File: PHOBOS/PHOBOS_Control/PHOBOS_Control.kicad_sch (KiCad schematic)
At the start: 85 parts, among them J1 Screw_Terminal_01x02, J2 Conn_01x06, J3 Conn_Coaxial, J4 Conn_01x03, J5 Conn_01x03, J6 USB4056-03-A_REVA2, SW4 KMR211GLFS, U1 SX1280IMLTRT, U2 TLV9351IDCKR, U3 W25Q128JVSIQ, U4 NCP1117-3.3_SOT223, U5 RP2040, U6 TLV9351IDCKR, U7 TLV9351IDCKR, U8 TLV9351IDCKR, Y1 ABM8-272-T3, Y2 C1E-52.000-10-1012-X-M

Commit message: mounting holes added and shape changed. design blocks utilized
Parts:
- removed C26: .8P, Capacitor_SMD:C_0402_1005Metric_Pad0.74x0.62mm_HandSolder, symbol Device:C
- removed C27, C28: 100n, Capacitor_SMD:C_0402_1005Metric_Pad0.74x0.62mm_HandSolder, symbol Device:C
- removed C29: 100p, Capacitor_SMD:C_0402_1005Metric_Pad0.74x0.62mm_HandSolder, symbol Device:C
- removed C7: 1.2p, Capacitor_SMD:C_0402_1005Metric_Pad0.74x0.62mm_HandSolder, symbol Device:C
- removed J2: Conn_01x06, Connector_JST:JST_PH_B6B-PH-K_1x06_P2.00mm_Vertical, symbol Connector_Generic:Conn_01x06
- removed J3: Conn_Coaxial, SMA_J_P_GF_RA_SM1:SAMTEC_SMA-J-P-GF-RA-SM1, symbol Connector:Conn_Coaxial
- removed Y2: C1E-52.000-10-1012-X-M, C1E-52.000-10-1012-X-M:XTAL_C1E-52.000-10-1012-X-M, symbol C1E-52.000-10-1012-X-M:C1E-52.000-10-1012-X-M
- added C0: .8P, Capacitor_SMD:C_0402_1005Metric_Pad0.74x0.62mm_HandSolder, symbol Device:C
- added C1: 1.2p, Capacitor_SMD:C_0402_1005Metric_Pad0.74x0.62mm_HandSolder, symbol Device:C
- added C10, C8: 100n, Capacitor_SMD:C_0402_1005Metric_Pad0.74x0.62mm_HandSolder, symbol Device:C
- added C3: 100p, Capacitor_SMD:C_0402_1005Metric_Pad0.74x0.62mm_HandSolder, symbol Device:C
- added H1, H2: MountingHole, MountingHole:MountingHole_3.2mm_M3, symbol Mechanical:MountingHole
- added J1: Conn_01x06, Connector_PinHeader_2.54mm:PinHeader_1x06_P2.54mm_Vertical, symbol Connector_Generic:Conn_01x06
- added J2: Conn_Coaxial, SMA_J_P_GF_RA_SM1:SAMTEC_SMA-J-P-GF-RA-SM1, symbol Connector:Conn_Coaxial
- added Y1: C1E-52.000-10-1012-X-M, C1E-52.000-10-1012-X-M:XTAL_C1E-52.000-10-1012-X-M, symbol C1E-52.000-10-1012-X-M:C1E-52.000-10-1012-X-M
- TP3, TP4, TP5, TP6: now not fitted; now left out of the parts list
- renumbered C3 to C11, C8 to C12, C10 to C14, C11 to C15, C14 to C16, C12 to C17, C15 to C18, C16 to C19, C24 to C20, C17 to C21, C25 to C22, C18 to C23, C19 to C24, C20 to C25, C30 to C26, C32 to C27, C34 to C28, C36 to C29, C21 to C30, C22 to C31, C31 to C32, C35 to C34, C37 to C35, C23 to C36, C1 to C7, D4 to D1, D1 to D2, D5 to D3, J6 to J3, J1 to J4, J4 to J6, R11 to R1, R3 to R10, R5 to R11, R25 to R13, R2 to R14, R4 to R16, R8 to R17, R13 to R18, R26 to R19, R32 to R2, R10 to R3, R9 to R4, R7 to R5, R23 to R6, R19 to R7, R21 to R8, R1 to R9, SW4 to SW1, TP2 to TP1, TP1 to TP2, U3 to U2, U4 to U3, U5 to U4, U2 to U5, Y1 to Y2
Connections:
- net +3V3: now also C10.1
- net ANTENNA: now also C3.2, J2.1 (In)
- net GND: now also C0.2, C1.2, C10.2, C8.2, J1.6 (Pin_6), J2.2 (Ext), J2.3, J2.4, J2.5, Y1.2 (GND), Y1.4 (GND__1)
- net MISO: now also J1.4 (Pin_4)
- net MOSI: now also J1.3 (Pin_3)
- net NSS: now also J1.1 (Pin_1)
- net RFIO: now also C0.1
- net SCK: now also J1.2 (Pin_2)
- net VBAT_IO: now also C8.1
- net XTA: now also Y1.1
- net XTB: now also Y1.3
- net at C4.1, L1.2, L2.1: now also C1.1; no longer C2.1
- net at C4.2, L2.2: now also C2.1, C3.1
- new net +3.3V: J1.5 (Pin_5)
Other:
- note removed: "Transceiver"

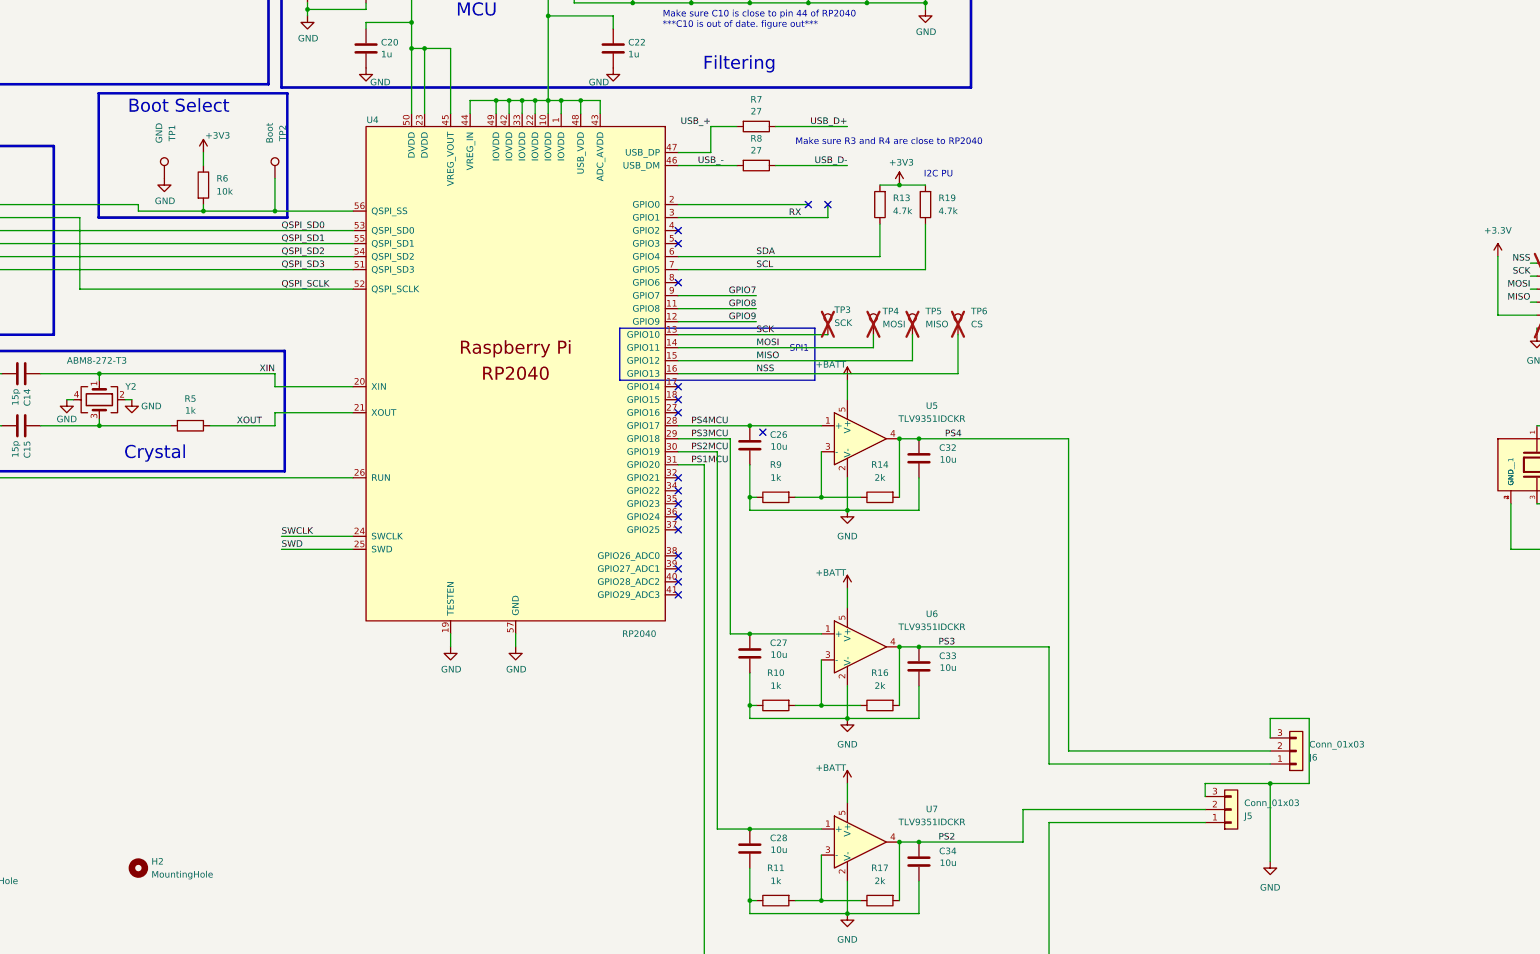
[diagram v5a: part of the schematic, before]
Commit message: PCB routed. perhaps add thermal reliefs on GND plane.
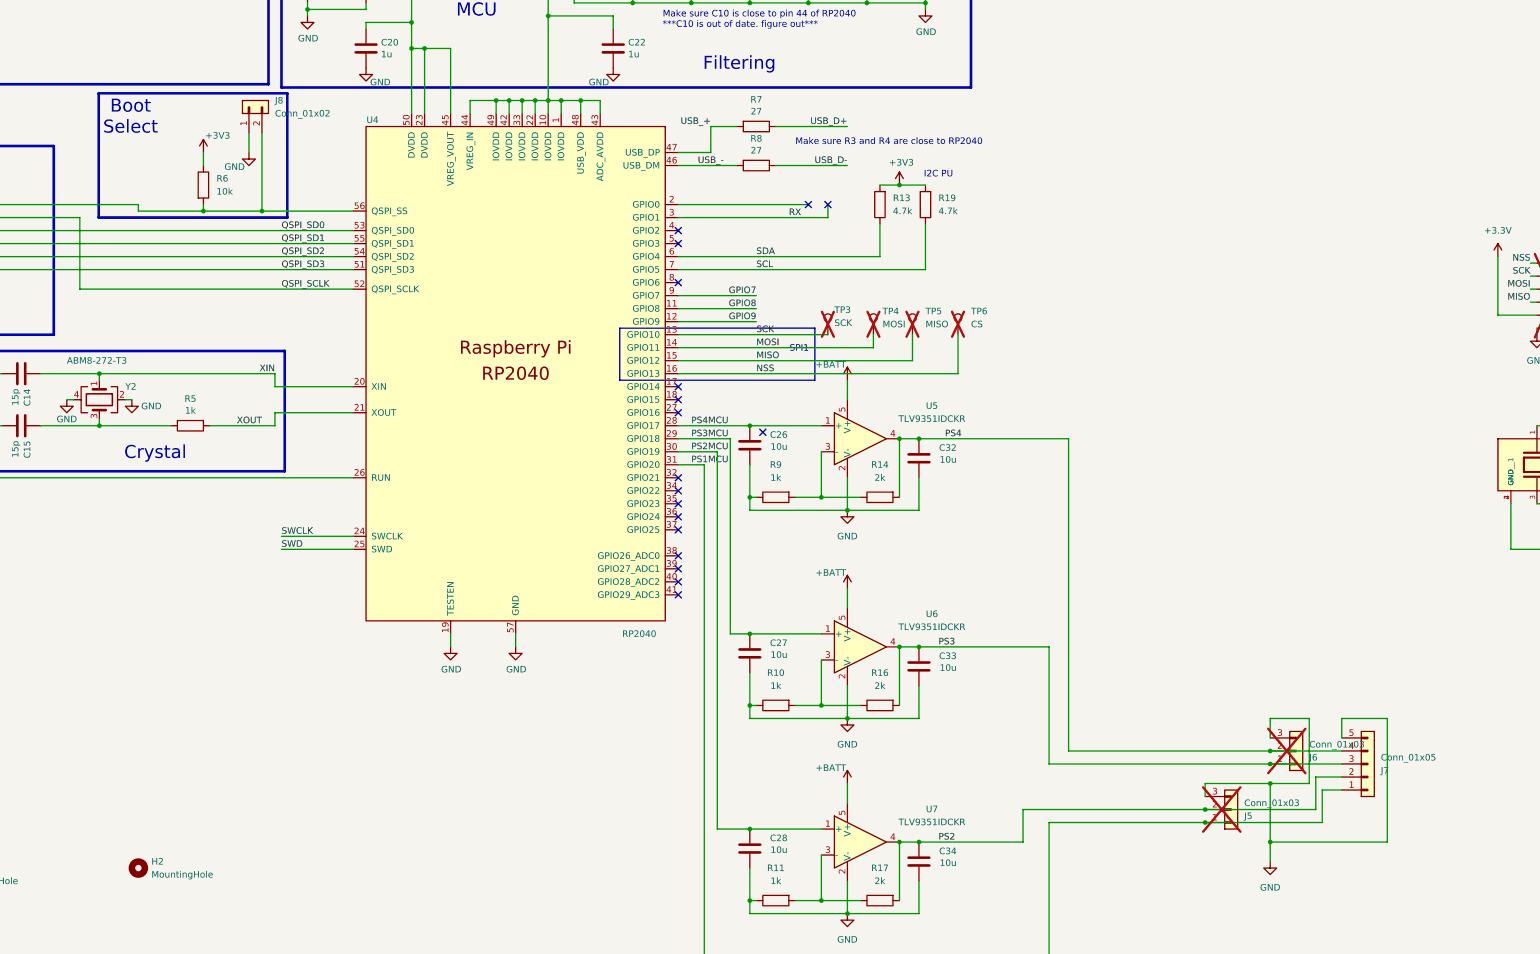
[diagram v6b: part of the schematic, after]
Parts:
- removed TP1: GND, TestPoint:TestPoint_Pad_D1.0mm, symbol Connector:TestPoint
- removed TP2: Boot, TestPoint:TestPoint_Pad_D1.0mm, symbol Connector:TestPoint
- added J7: Conn_01x05, Connector_JST:JST_PH_B5B-PH-K_1x05_P2.00mm_Vertical, symbol Connector_Generic:Conn_01x05
- added J8: Conn_01x02, Connector_PinHeader_2.54mm:PinHeader_1x02_P2.54mm_Vertical, symbol Connector_Generic:Conn_01x02
- J5, J6: now not fitted; now left out of the parts list
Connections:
- net GND: now also J7.5 (Pin_5), J8.1 (Pin_1)
- net PS1: now also J7.1 (Pin_1)
- net PS2: now also J7.2 (Pin_2)
- net PS3: now also J7.3 (Pin_3)
- net PS4: now also J7.4 (Pin_4)
- net QSPI_SS: now also J8.2 (Pin_2)

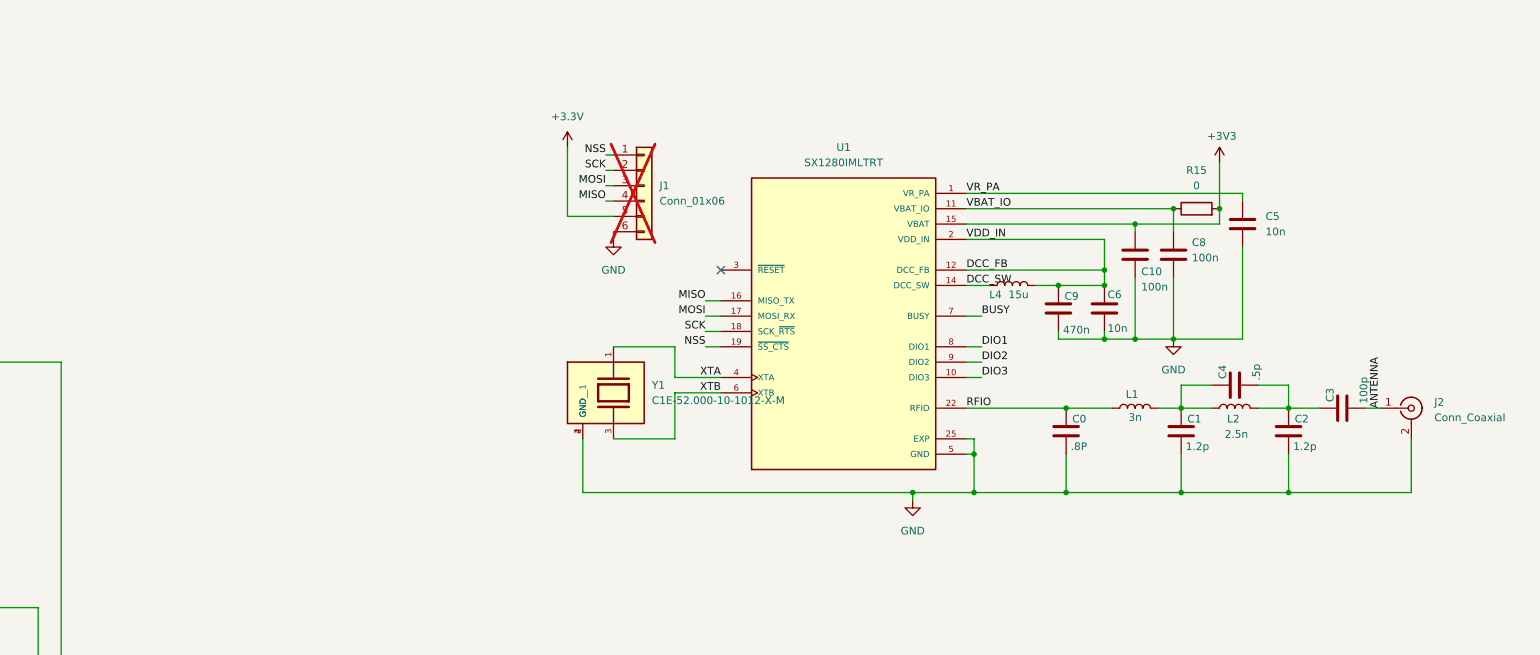
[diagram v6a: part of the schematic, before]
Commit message: drc updated. 33 usb error. silkscreen warnings
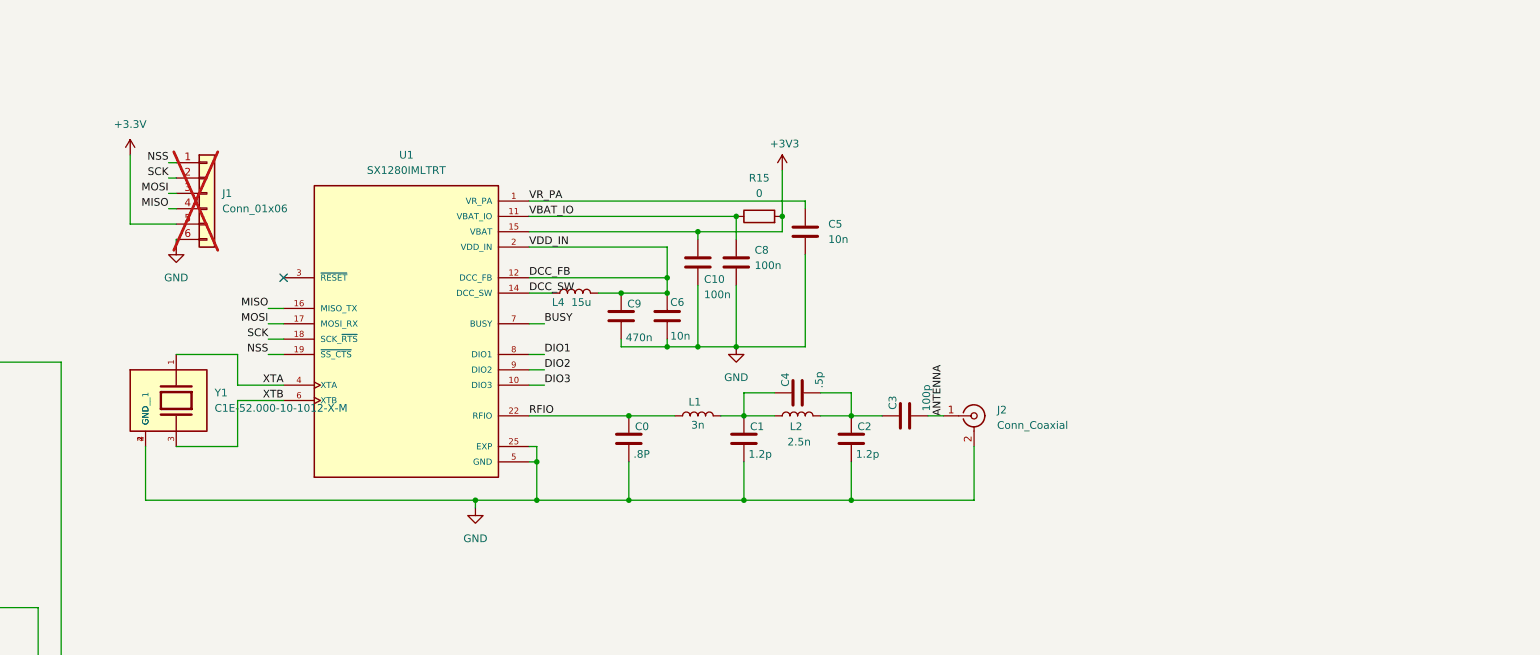
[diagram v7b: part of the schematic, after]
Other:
- moved on the sheet: C0, C1, C10, C2, C3, C4, C5, C6, C8, C9, J1, J2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

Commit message: RF Board schematic began
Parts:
- J2: value Conn_Coaxial -> RF_OUT
- J7: value Conn_01x05 -> PS_CONTROL
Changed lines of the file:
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@@
 			)
 		)
-		(property "Value" "Conn_01x05"
+		(property "Value" "PS_CONTROL"
 			(at 455.93 297.1801 0)
 			(show_name no)
@@
 		(fields_autoplaced yes)
 		(property "Reference" "J2"
-			(at 549.91 242.8631 0)
+			(at 548.64 242.8631 0)
 			(show_name no)
 			(do_not_autoplace no)
@@
 			)
 		)
-		(property "Value" "Conn_Coaxial"
-			(at 549.91 245.4031 0)
+		(property "Value" "RF_OUT"
+			(at 548.64 245.4031 0)
 			(show_name no)
 			(do_not_autoplace no)
